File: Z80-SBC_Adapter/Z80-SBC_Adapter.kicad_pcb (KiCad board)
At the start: 2 copper layers, 32.6 x 21.5 mm, 4 parts, among them J1 Z80-MBC2 direct, J4 Mini-DIN-6, J7 Z80-MBC2 direct

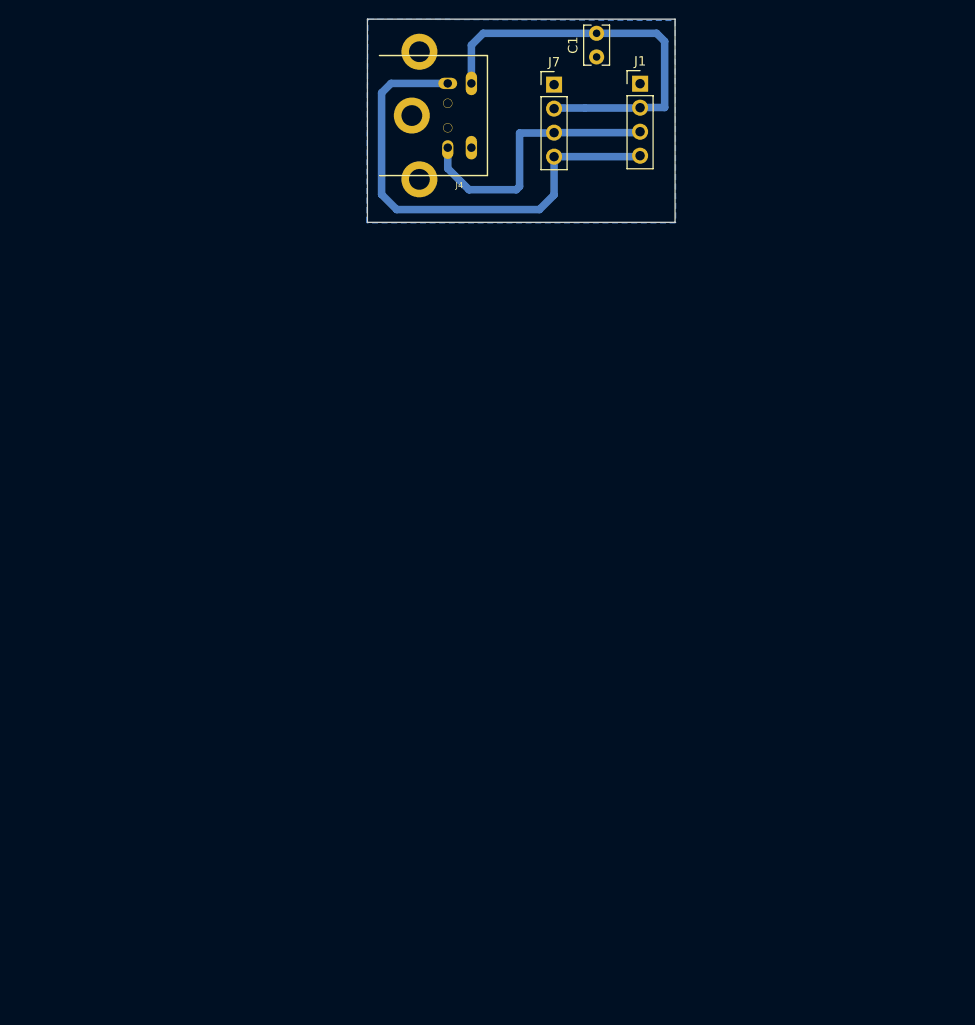
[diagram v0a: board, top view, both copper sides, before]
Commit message: Geänderte Adapterplatine mit Readme
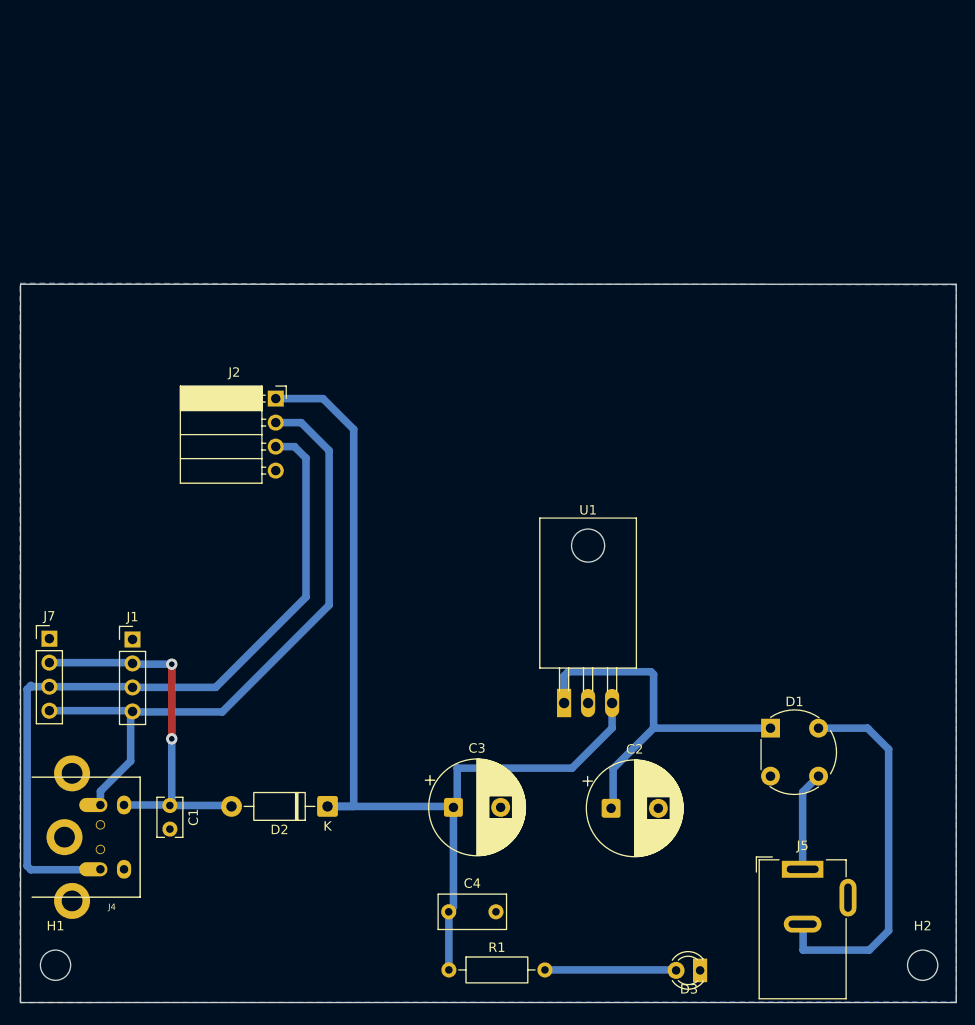
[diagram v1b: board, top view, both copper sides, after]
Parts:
- added C2: 100u / 16V, Capacitor_THT:CP_Radial_D10.0mm_P5.00mm, F.Cu at (132.6, 151.6)
- added C3: 47u / 16V, Capacitor_THT:CP_Radial_D10.0mm_P5.00mm, F.Cu at (116.0, 151.5)
- added C4: 0.1u, Capacitor_THT:C_Rect_L7.0mm_W3.5mm_P5.00mm, F.Cu at (115.5, 162.6)
- added D1: 25V / 500mA, Diode_THT:Diode_Bridge_Round_D8.9mm, F.Cu at (149.5, 143.1)
- added D2: 1N5817, Diode_THT:D_DO-41_SOD81_P10.16mm_Horizontal, F.Cu at (102.6, 151.4)
- added D3: ON/OFF, LED_THT:LED_D3.0mm, F.Cu at (142.1, 168.8)
- added H1: MountingHole, MountingHole:MountingHole_3.2mm_M3, F.Cu at (73.8, 168.2)
- added H2: MountingHole, MountingHole:MountingHole_3.2mm_M3, F.Cu at (165.6, 168.2)
- added J2: RS232 Adapterplatine, Connector_PinSocket_2.54mm:PinSocket_1x04_P2.54mm_Horizontal, F.Cu at (97.2, 108.2)
- added J5: 5,4x2,1mm 7 - 9V DC/AC, Connector_BarrelJack:BarrelJack_Wuerth_6941xx301002, F.Cu at (152.9, 158.1)
- added R1: 470, Resistor_THT:R_Axial_DIN0207_L6.3mm_D2.5mm_P10.16mm_Horizontal, F.Cu at (115.5, 168.7)
- added U1: L7805, Package_TO_SOT_THT:TO-220-3_Horizontal_TabDown, F.Cu at (127.7, 140.5)
- J7: value Z80-MBC2 direct -> Z80-MBC2 Board
- moved C1 91.2 mm to (86.0, 151.3), turned to -90 degrees
- moved J4 84.7 mm to (70.1, 154.7)
- moved J1 79.6 mm to (82.0, 133.7)
- moved J7 79.3 mm to (73.2, 133.7)
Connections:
- C1 pad 1: GND -> Net-(D2-A)
- C1 pad 2: Net-(J1-Pin_2) -> GND
- J1 pad 2: Net-(J1-Pin_2) -> Net-(D2-A)
- J4 pad 6: Net-(J1-Pin_2) -> Net-(D2-A)
- J7 pad 2: Net-(J1-Pin_2) -> Net-(D2-A)
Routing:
- net 5VDC: track 0.00 -> 108.2 mm
- net Net-(J1-Pin_3): track 29.3 -> 78.8 mm
- net Net-(J1-Pin_2): track 44.1 -> 0.00 mm
- net Net-(D1-+): track 0.00 -> 41.0 mm
- net Net-(J5-MountPin): track 0.00 -> 40.2 mm
- net Net-(D2-A): track 0.00 -> 39.6 mm, vias 0 -> 2
- net Net-(J1-Pin_4): track 50.9 -> 68.9 mm
- net Net-(D3-A): track 0.00 -> 13.9 mm
- net Net-(D1-Pad3): track 0.00 -> 10.5 mm
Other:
- board size 32.6 x 21.5 mm -> 99 x 76 mm

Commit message: Adapterplatine überarbeitet
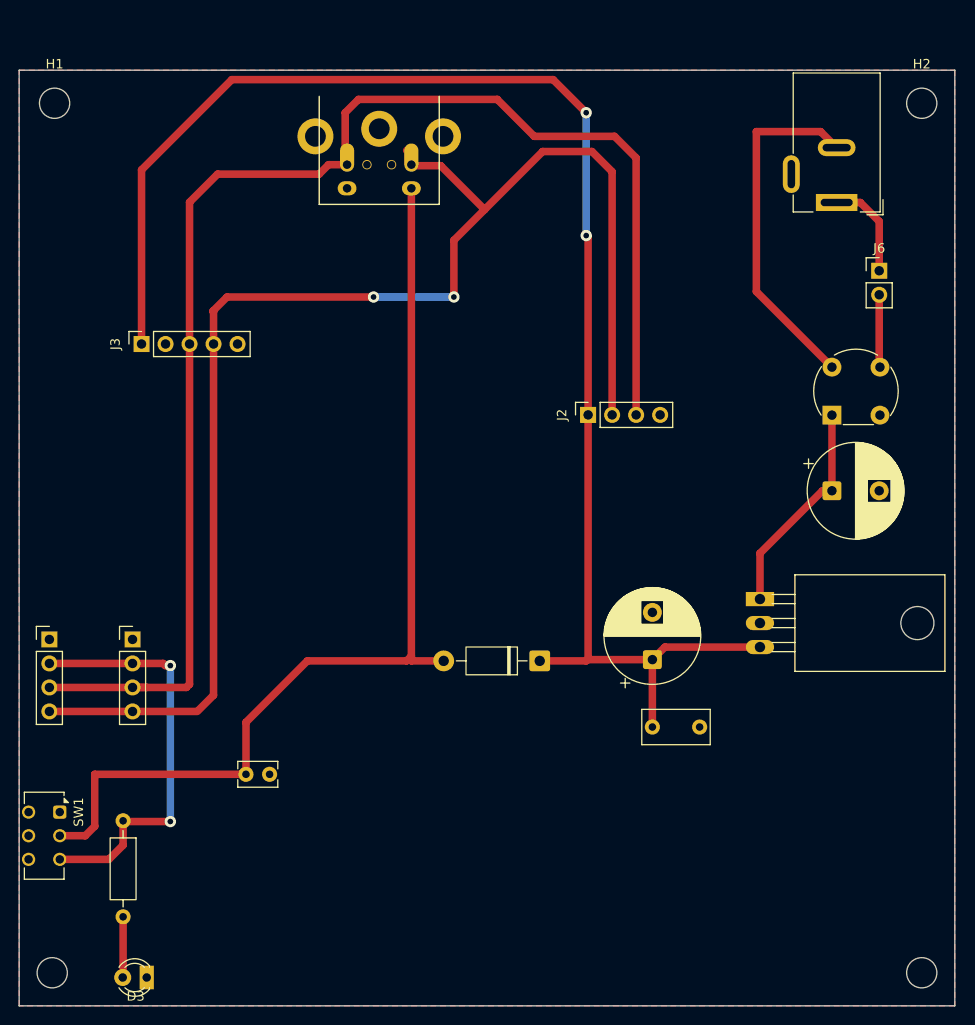
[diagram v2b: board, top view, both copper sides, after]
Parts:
- added H1: MountingHole, MountingHole:MountingHole_3.2mm_M3, F.Cu at (73.8, 77.0)
- added H2: MountingHole, MountingHole:MountingHole_3.2mm_M3, F.Cu at (165.5, 77.0)
- added J3: USB-Serial-Adapter Board, Connector_PinSocket_2.54mm:PinSocket_1x05_P2.54mm_Vertical, F.Cu at (83.0, 102.5)
- added J6: Power on / off, Connector_PinHeader_2.54mm:PinHeader_1x02_P2.54mm_Vertical, F.Cu at (161.0, 94.7)
- added SW1: On Off, Button_Switch_THT:SW_CK_JS202011AQN_DPDT_Angled, F.Cu at (74.3, 152.0)
- J2: footprint Connector_PinSocket_2.54mm:PinSocket_1x04_P2.54mm_Horizontal -> Connector_PinSocket_2.54mm:PinSocket_1x04_P2.54mm_Vertical
- moved J4 88.3 mm to (108.1, 75.0), turned to 0 degrees
- moved J5 70.6 mm to (156.5, 87.5), turned to 180 degrees
- moved D3 58.6 mm to (83.5, 169.5)
- moved C2 40.9 mm to (156.0, 118.0)
- moved R1 37.9 mm to (81.0, 152.9), turned to -90 degrees
- moved D1 33.8 mm to (156.0, 110.0), turned to 90 degrees
- moved J2 33.1 mm to (130.2, 110.0), turned to 90 degrees
- moved C4 29.1 mm to (137.0, 143.0)
- moved D2 27.2 mm to (125.1, 136.0)
- moved C3 26.2 mm to (137.0, 135.9), turned to 90 degrees
- moved U1 23.5 mm to (148.4, 129.5), turned to -90 degrees
- moved C1 8.70 mm to (94.0, 148.0), turned to 0 degrees
- moved H1 0.87 mm to (73.5, 169.0)
- moved H2 0.81 mm to (165.5, 169.0)
- moved J7 0.08 mm to (73.2, 133.7)
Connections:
- D1 pad 3: Net-(D1-Pad3) -> Net-(J6-Pin_2)
- J1 pad 2: Net-(D2-A) -> Net-(J1-Pin_2)
- J5 pad 1: Net-(D1-Pad3) -> Net-(J6-Pin_1)
- J7 pad 2: Net-(D2-A) -> Net-(J1-Pin_2)
- R1 pad 1: 5VDC -> Net-(J1-Pin_2)
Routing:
- net Net-(J1-Pin_4): track 68.9 -> 147.8 mm, vias 0 -> 2
- net Net-(J1-Pin_3): track 78.8 -> 152.1 mm
- net Net-(D2-A): track 39.6 -> 104.9 mm, vias 2 -> 0
- net 5VDC: track 108.2 -> 160.0 mm, vias 0 -> 2
- net Net-(J1-Pin_2): track 0.00 -> 44.3 mm, vias 0 -> 2
- net Net-(D1-+): track 41.0 -> 23.2 mm
- net Net-(J6-Pin_1): track 0.00 -> 10.6 mm
- net Net-(D1-Pad3): track 10.5 -> 0.00 mm
- net Net-(J6-Pin_2): track 0.00 -> 7.69 mm
- net Net-(D3-A): track 13.9 -> 6.44 mm
- net Net-(J5-MountPin): track 40.2 -> 37.4 mm
- added copper zone on F.Cu, net GND
- removed copper zone on B.Cu, net GND
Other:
- board size 99 x 76 mm -> 99 x 99 mm

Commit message: Layout geändert bei Adapterplatine MSBC-z80
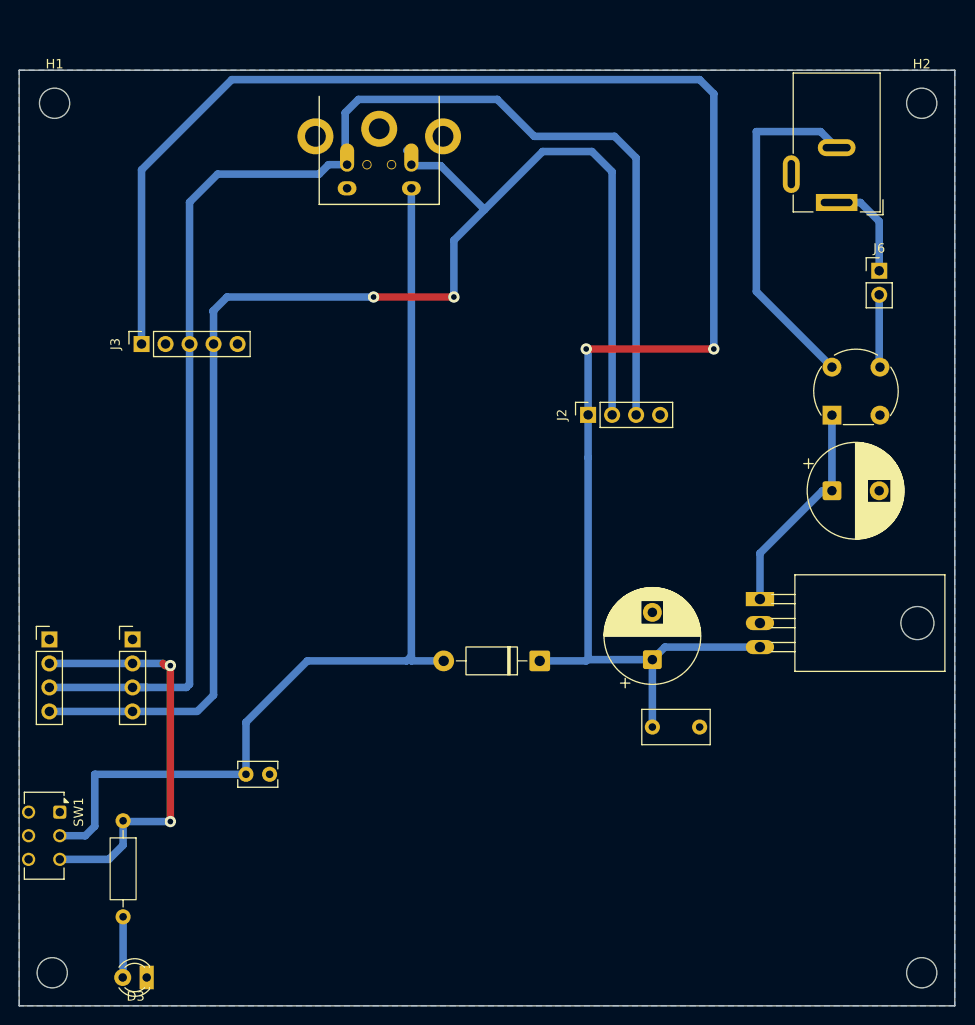
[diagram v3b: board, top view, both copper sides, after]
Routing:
- net 5VDC: track 160.0 -> 188.2 mm
- added copper zone on B.Cu, net GND
- removed copper zone on F.Cu, net GND
